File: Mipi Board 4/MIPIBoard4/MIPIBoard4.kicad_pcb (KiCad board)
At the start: 4 copper layers, 55.2 x 46.7 mm, 69 parts, among them J1 Power/Control Top, J2 Bank A Top, J3 Bank B Top, J4 MIPI1, J5 MIPI2, J6 Bank A Bottom, J7 Bank B Bottom, J8 Power/Control Bottom, U1 LM339, U2 LM339, U3 LM339, U4 TLV3605RVKR, U5 TLV3605RVKR, U6 TLV3605RVKR, U7 TLV3605RVKR, U8 TLV3605RVKR, U9 TLV3605RVKR

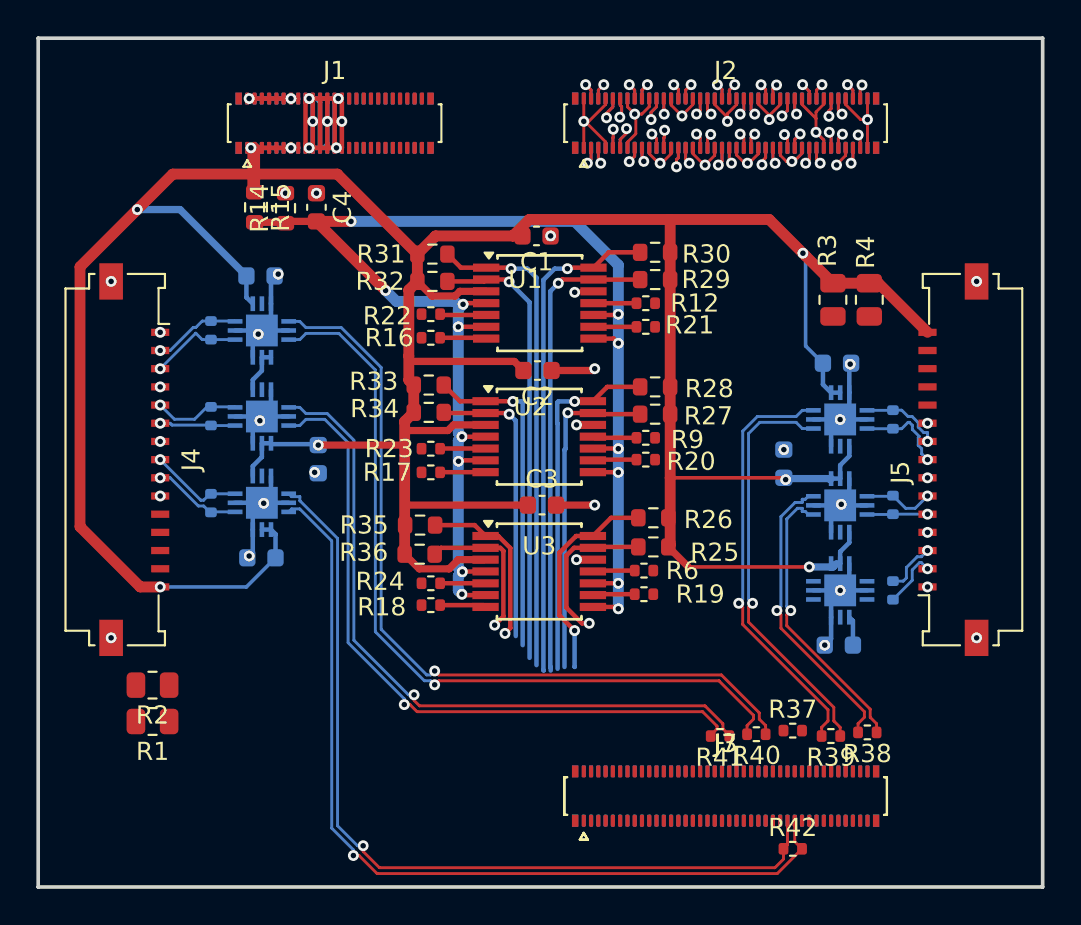
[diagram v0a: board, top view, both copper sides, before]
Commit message: One side length matched
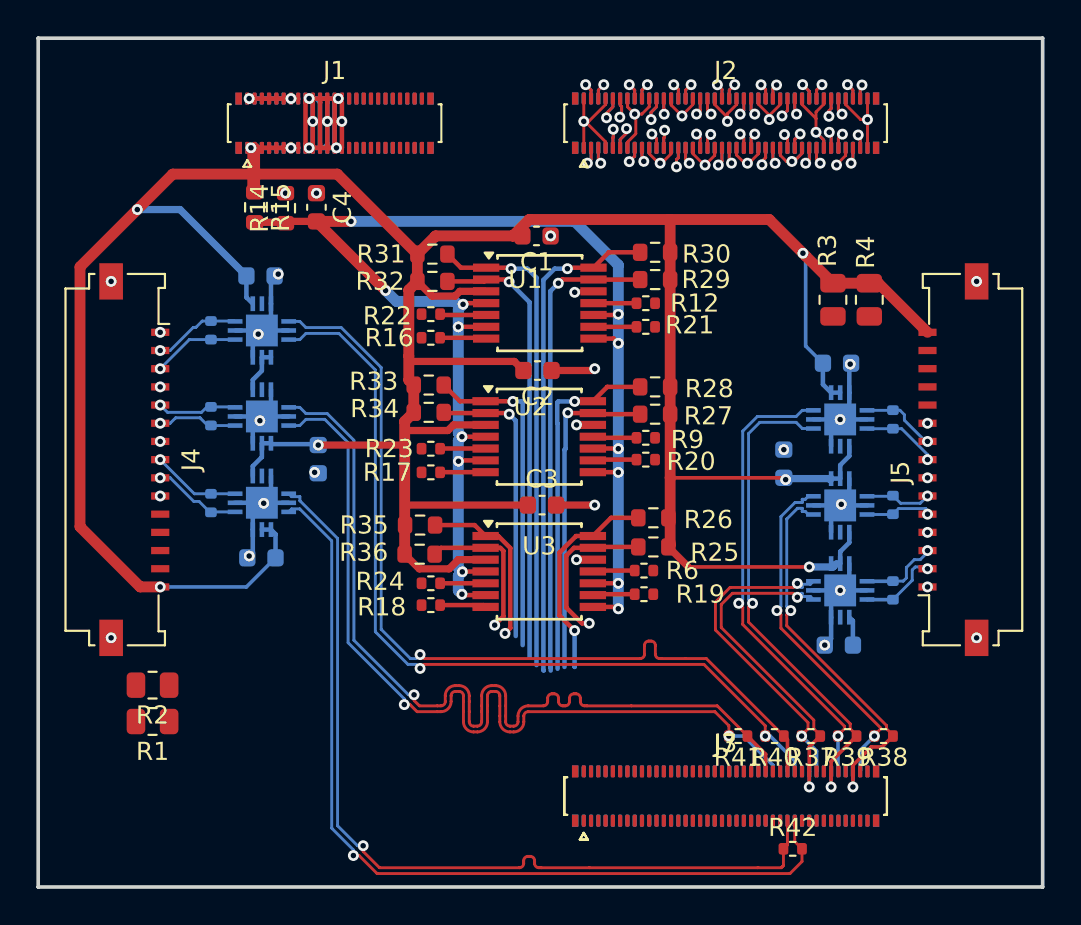
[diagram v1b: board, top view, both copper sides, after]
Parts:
- moved R37 1.04 mm to (92.7, 87.7), turned to 180 degrees
- moved R40 1.00 mm to (90.7, 87.7)
- moved R41 1.00 mm to (88.7, 87.7)
- moved R38 0.92 mm to (96.7, 87.7)
- moved R39 0.90 mm to (94.7, 87.7)
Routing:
- net 34_L8/1.5B_N: track 0.00 -> 19.1 mm, vias 0 -> 2
- net 34_L8/1.5B_P: track 0.00 -> 18.0 mm, vias 0 -> 2
- net 34_L4/1.5B_N: track 38.5 -> 50.5 mm
- net 34_L4/1.5B_P: track 38.0 -> 49.0 mm, vias 1 -> 2
- net 34_L6/1.5B_N: track 15.9 -> 21.4 mm, vias 1 -> 2
- net 34_L9/1.5B_N: track 22.9 -> 27.5 mm, vias 1 -> 2
- net 34_L7/1.5B_N: track 44.7 -> 48.8 mm
- net 34_L7/1.5B_P: track 44.2 -> 47.2 mm, vias 1 -> 2
- net 34_L6/1.5B_P: track 16.4 -> 19.3 mm, vias 1 -> 2
- net 34_L9/1.5B_P: track 23.4 -> 25.7 mm, vias 1 -> 2
- net Cam2_D0_P: track 2.93 -> 4.42 mm
- net Cam2_D0_N: track 3.22 -> 4.45 mm
- net 34_L3/1.5B_N: track 47.7 -> 48.7 mm
- net Cam2_CK_N: track 4.99 -> 4.20 mm

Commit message: both sides length matched
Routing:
- net 34_L8/1.5B_P: track 18.0 -> 25.6 mm
- net 34_L6/1.5B_P: track 19.3 -> 26.5 mm
- net 34_L8/1.5B_N: track 19.1 -> 25.7 mm
- net 34_L6/1.5B_N: track 21.4 -> 26.6 mm
- net 34_L9/1.5B_N: track 27.5 -> 26.0 mm

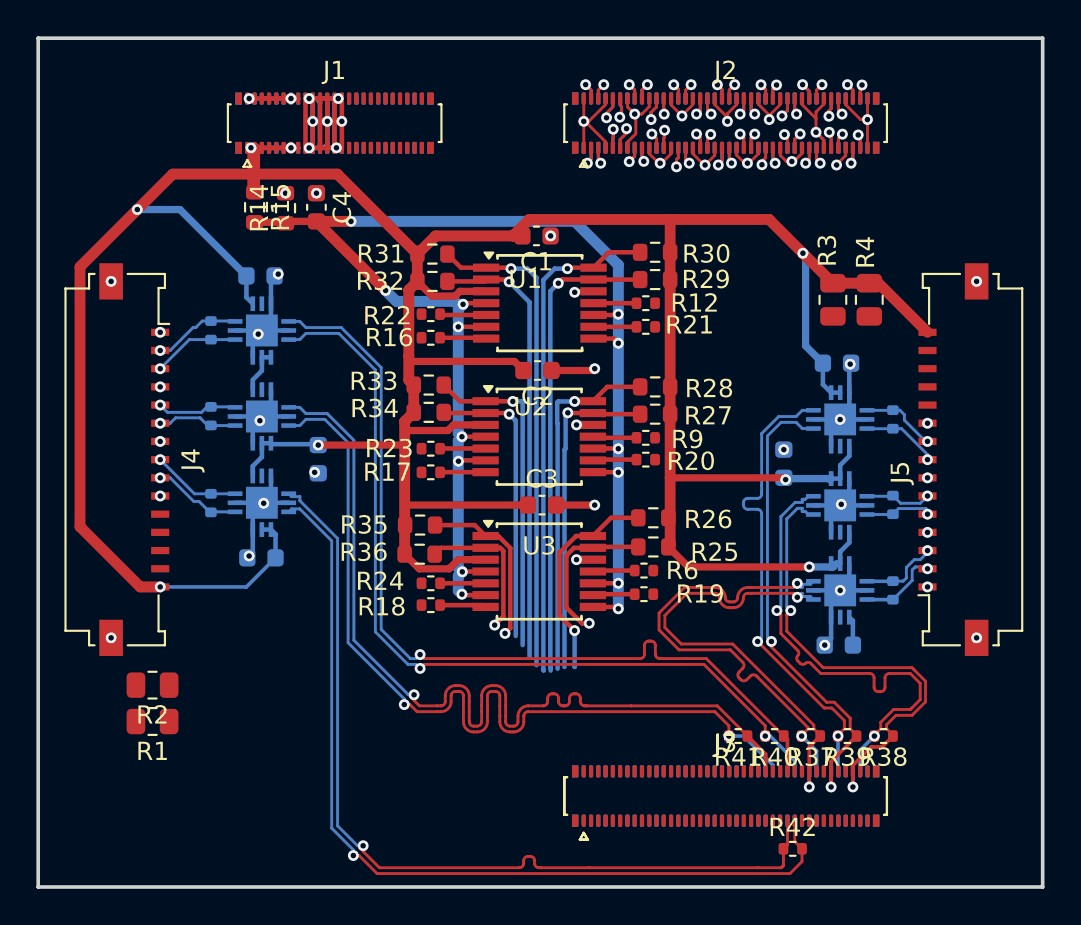
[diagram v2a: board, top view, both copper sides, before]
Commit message: everything wired lengths were messed up
Need to rematch the lengths for MIPI2
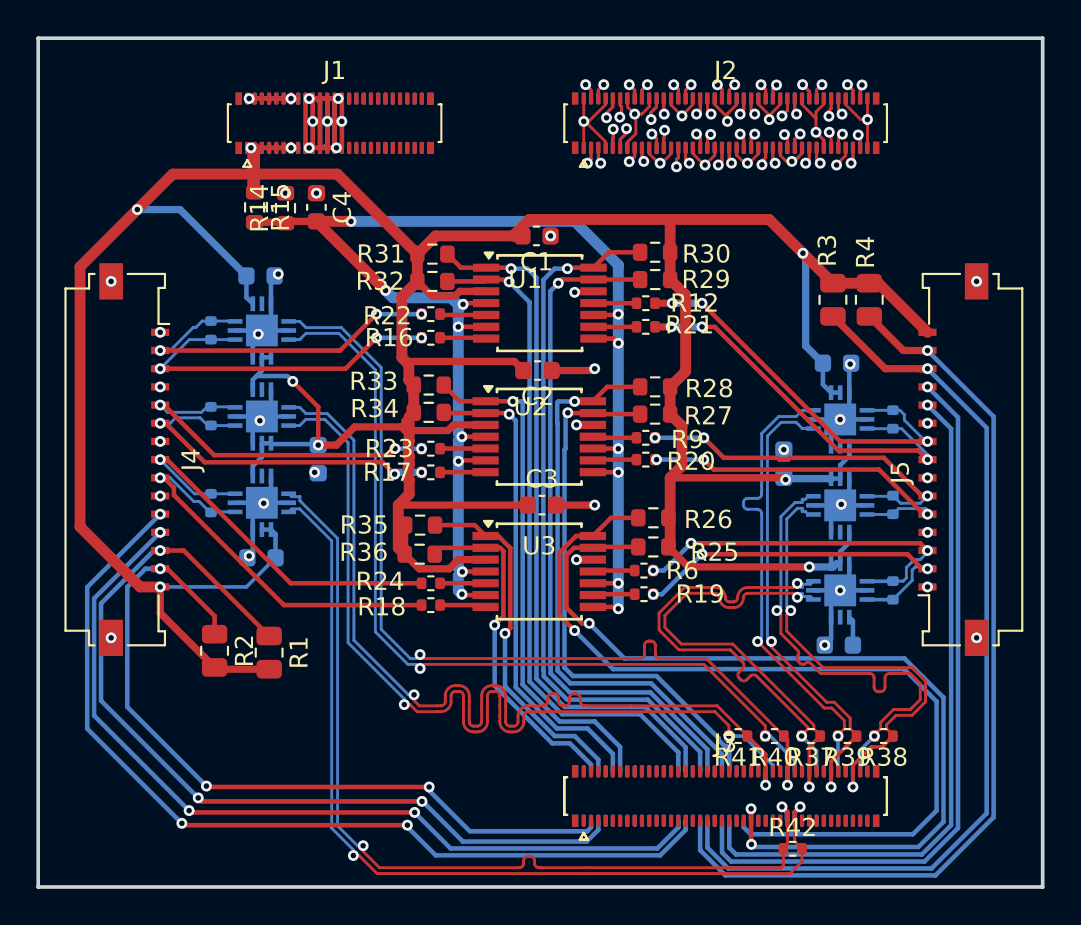
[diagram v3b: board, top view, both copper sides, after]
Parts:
- moved R1 7.45 mm to (62.9, 83.1), turned to -90 degrees
- moved R2 3.90 mm to (59.9, 83.0), turned to -90 degrees
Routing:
- net 35_K5_SDA/1.4D: track 0.00 -> 50.8 mm, vias 0 -> 1
- net 35_E6_SCL/1.4A: track 0.00 -> 50.8 mm, vias 0 -> 1
- net 14_L17_P/1.2C: track 0.00 -> 50.4 mm, vias 0 -> 3
- net 14_L21_P/1.2D: track 0.00 -> 49.1 mm, vias 0 -> 3
- net 14_L17_N/1.2C: track 0.00 -> 47.6 mm, vias 0 -> 3
- net 14_L21_N/1.2D: track 0.00 -> 42.8 mm, vias 0 -> 3
- net 14_L13_MRCC_P/1.2C: track 8.63 -> 50.5 mm, vias 1 -> 3
- net 14_L14_SRCC_N/1.2C: track 0.00 -> 40.7 mm, vias 0 -> 1
- net 14_L14_SRCC_P/1.2C: track 0.00 -> 38.1 mm, vias 0 -> 1
- net 14_L13_MRCC_N/1.2C: track 11.8 -> 48.9 mm
- net Cam2_CK_P: track 4.22 -> 22.3 mm, vias 1 -> 3
- net Cam2_CK_N: track 4.20 -> 22.2 mm, vias 1 -> 3
- net Cam1_CK_P: track 4.91 -> 22.4 mm
- net Cam1_CK_N: track 4.90 -> 22.1 mm
- net Cam2_D1_P: track 3.68 -> 20.1 mm, vias 1 -> 3
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
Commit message: retuned lengths
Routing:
- net 34_L4/1.5B_P: track 49.0 -> 52.3 mm
- net 34_L7/1.5B_P: track 47.2 -> 50.5 mm

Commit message: finished wiring
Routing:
- net GND: track 161.3 -> 247.6 mm, vias 51 -> 60
- net +3V3: track 237.3 -> 259.7 mm, vias 9 -> 10
- net LED2/1.5D: track 0.00 -> 2.16 mm, vias 0 -> 1
- net PROGRAM_B/6.5B: track 0.00 -> 1.72 mm, vias 0 -> 1
- net LED5/1.5D: track 0.00 -> 1.71 mm, vias 0 -> 1
- net AVREF_P/3.2D: track 0.00 -> 1.71 mm, vias 0 -> 1
- net TDI/6.4B: track 0.00 -> 1.69 mm, vias 0 -> 1
- net TMS/6.4B: track 0.00 -> 1.69 mm, vias 0 -> 1
- net LED3/1.5D: track 0.00 -> 1.69 mm, vias 0 -> 1
- net DONE/6.5B: track 0.00 -> 1.69 mm, vias 0 -> 1
- net LED0/1.5D: track 0.00 -> 1.65 mm, vias 0 -> 1
- net RESET/1.5D: track 0.00 -> 1.52 mm, vias 0 -> 1
- net TDO/6.4B: track 0.00 -> 1.52 mm, vias 0 -> 1
- net TCK/6.4B: track 0.00 -> 1.52 mm, vias 0 -> 1
- net LED7/1.5D: track 0.00 -> 1.51 mm, vias 0 -> 1
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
